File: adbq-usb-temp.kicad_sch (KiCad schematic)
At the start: 74 parts, among them J4 USB_C_Receptacle_USB2.0_14P, Q1 Q_NMOS, Q2 Q_NMOS, Q3 Q_NMOS, SW1 SW_Push, SW2 TestPoint, SW3 TestPoint, SW4 TestPoint, U1 ESP32-S3FH4R2, U14 TMP117AIDRV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

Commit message: schem: update MOSFETs pin numbers
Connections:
- net GND: now also Q1.2 (S), Q2.2 (S), Q3.2 (S); no longer Q1.S, Q2.S, Q3.S
- net at R15.1: now also Q1.1 (G); no longer Q1.G
- net at R11.1: now also Q3.1 (G); no longer Q3.G
- net at U3.8 (DIG3): now also Q3.3 (D); no longer Q3.D
- net at U3.12 (DIG1): now also Q1.3 (D); no longer Q1.D
- net at U3.9 (DIG2): now also Q2.3 (D); no longer Q2.D
- net at R9.1: now also Q2.1 (G); no longer Q2.G
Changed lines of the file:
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@@
 	)
 	(symbol
-		(lib_id "Device:Q_NMOS")
-		(at 111.76 111.76 0)
-		(mirror y)
-		(unit 1)
-		(exclude_from_sim no)
-		(in_bom yes)
-		(on_board yes)
-		(dnp no)
-		(property "Reference" "Q3"
-			(at 107.188 108.966 0)
-			(effects
-				(font
-					(size 1.27 1.27)
-				)
-				(justify left)
-			)
-		)
-		(property "Value" "Q_NMOS"
-			(at 105.41 113.0299 0)
-			(effects
-				(font
-					(size 1.27 1.27)
-				)
-				(justify left)
-				(hide yes)
-			)
-		)
-		(property "Footprint" "Package_TO_SOT_SMD:SOT-323_SC-70"
-			(at 106.68 109.22 0)
-			(effects
-				(font
-					(size 1.27 1.27)
-				)
-				(hide yes)
-			)
-		)
-		(property "Datasheet" "~"
-			(at 111.76 111.76 0)
-			(effects
-				(font
-					(size 1.27 1.27)
-				)
-				(hide yes)
-			)
-		)
-		(property "Description" "N-MOSFET transistor"
-			(at 111.76 111.76 0)
-			(effects
-				(font
-					(size 1.27 1.27)
-				)
-				(hide yes)
-			)
-		)
-		(property "Basic" "E"
-			(at 111.76 111.76 0)
-			(effects
-				(font
-					(size 1.27 1.27)
-				)
-				(hide yes)
-			)
-		)
-		(property "JLCPCB Part #" "C28646265"
-			(at 111.76 111.76 0)
-			(effects
-				(font
-					(size 1.27 1.27)
-				)
-				(hide yes)
-			)
-		)
-		(property "Manufacturer" "hongjiacheng"
-			(at 111.76 111.76 0)
-			(effects
-				(font
-					(size 1.27 1.27)
-				)
-				(hide yes)
-			)
-		)
-		(property "Manufacturer Part Number" "BSS138W"
-			(at 111.76 111.76 0)
-			(effects
-				(font
-					(size 1.27 1.27)
-				)
-				(hide yes)
-			)
-		)
-		(pin "S"
-		)
-		(pin "G"
-		)
-		(pin "D"
-		)
-		(instances
-			(project "adbq-usb-temp"
-				(path "/683f6451-7bb7-4686-955a-dbaefe964302"
-					(reference "Q3")
-					(unit 1)
-				)
-			)
-		)
-	)
-	(symbol
 		(lib_id "power:GND")
 		(at 31.75 190.5 0)
@@
 	)
 	(symbol
+		(lib_id "Device:Q_NMOS")
+		(at 111.76 111.76 0)
+		(mirror y)
+		(unit 1)
+		(exclude_from_sim no)
+		(in_bom yes)
+		(on_board yes)
+		(dnp no)
+		(property "Reference" "Q3"
+			(at 107.188 108.966 0)
+			(effects
+				(font
+					(size 1.27 1.27)
+				)
+				(justify left)
+			)
+		)
+		(property "Value" "Q_NMOS"
+			(at 105.41 113.0299 0)
+			(effects
+				(font
+					(size 1.27 1.27)
+				)
+				(justify left)
+				(hide yes)
+			)
+		)
+		(property "Footprint" "Package_TO_SOT_SMD:SOT-323_SC-70"
+			(at 106.68 109.22 0)
+			(effects
+				(font
+					(size 1.27 1.27)
+				)
+				(hide yes)
+			)
+		)
+		(property "Datasheet" "~"
+			(at 111.76 111.76 0)
+			(effects
+				(font
+					(size 1.27 1.27)
+				)
+				(hide yes)
+			)
+		)
+		(property "Description" "N-MOSFET transistor"
+			(at 111.76 111.76 0)
+			(effects
+				(font
+					(size 1.27 1.27)
+				)
+				(hide yes)
+			)
+		)
+		(property "Basic" "E"
+			(at 111.76 111.76 0)
+			(effects
+				(font
+					(size 1.27 1.27)
+				)
+				(hide yes)
+			)
+		)
+		(property "JLCPCB Part #" "C28646265"
+			(at 111.76 111.76 0)
+			(effects
+				(font
+					(size 1.27 1.27)
+				)
+				(hide yes)
+			)
+		)
+		(property "Manufacturer" "hongjiacheng"
+			(at 111.76 111.76 0)
+			(effects
+				(font
+					(size 1.27 1.27)
+				)
+				(hide yes)
+			)
+		)
+		(property "Manufacturer Part Number" "BSS138W"
+			(at 111.76 111.76 0)
+			(effects
+				(font
+					(size 1.27 1.27)
+				)
+				(hide yes)
+			)
+		)
+		(pin "3"
+		)
+		(pin "2"
+		)
+		(pin "1"
+		)
+		(instances
+			(project "adbq-usb-temp"
+				(path "/683f6451-7bb7-4686-955a-dbaefe964302"
+					(reference "Q3")
+					(unit 1)
+				)
+			)
+		)
+	)
+	(symbol
 		(lib_id "power:GND")
 		(at 38.1 50.8 0)
@@
 			)
 		)
-		(pin "S"
+		(pin "3"
 		)
-		(pin "G"
+		(pin "2"
 		)
-		(pin "D"
+		(pin "1"
 		)
 		(instances
@@
 	)
 	(symbol
+		(lib_id "Device:Q_NMOS")
+		(at 97.79 111.76 0)
+		(mirror y)
+		(unit 1)
+		(exclude_from_sim no)
+		(in_bom yes)
+		(on_board yes)
+		(dnp no)
+		(property "Reference" "Q2"
+			(at 93.218 108.966 0)
+			(effects
+				(font
+					(size 1.27 1.27)
+				)
+				(justify left)
+			)
+		)
+		(property "Value" "Q_NMOS"
+			(at 91.44 113.0299 0)
+			(effects
+				(font
+					(size 1.27 1.27)
+				)
+				(justify left)
+				(hide yes)
+			)
+		)
+		(property "Footprint" "Package_TO_SOT_SMD:SOT-323_SC-70"
+			(at 92.71 109.22 0)
+			(effects
+				(font
+					(size 1.27 1.27)
+				)
+				(hide yes)
+			)
+		)
+		(property "Datasheet" "~"
+			(at 97.79 111.76 0)
+			(effects
+				(font
+					(size 1.27 1.27)
+				)
+				(hide yes)
+			)
+		)
+		(property "Description" "N-MOSFET transistor"
+			(at 97.79 111.76 0)
+			(effects
+				(font
+					(size 1.27 1.27)
+				)
+				(hide yes)
+			)
+		)
+		(property "Basic" "E"
+			(at 97.79 111.76 0)
+			(effects
+				(font
+					(size 1.27 1.27)
+				)
+				(hide yes)
+			)
+		)
+		(property "JLCPCB Part #" "C28646265"
+			(at 97.79 111.76 0)
+			(effects
+				(font
+					(size 1.27 1.27)
+				)
+				(hide yes)
+			)
+		)
+		(property "Manufacturer" "hongjiacheng"
+			(at 97.79 111.76 0)
+			(effects
+				(font
+					(size 1.27 1.27)
+				)
+				(hide yes)
+			)
+		)
+		(property "Manufacturer Part Number" "BSS138W"
+			(at 97.79 111.76 0)
+			(effects
+				(font
+					(size 1.27 1.27)
+				)
+				(hide yes)
+			)
+		)
+		(pin "3"
+		)
+		(pin "2"
+		)
+		(pin "1"
+		)
+		(instances
+			(project "adbq-usb-temp"
+				(path "/683f6451-7bb7-4686-955a-dbaefe964302"
+					(reference "Q2")
+					(unit 1)
+				)
+			)
+		)
+	)
+	(symbol
 		(lib_id "Device:C")
 		(at 133.35 44.45 270)
@@
 					(unit 1)
 				)
-			)
-		)
-	)
-	(symbol
-		(lib_id "Device:Q_NMOS")
-		(at 97.79 111.76 0)
-		(mirror y)
-		(unit 1)
-		(exclude_from_sim no)
-		(in_bom yes)
-		(on_board yes)
-		(dnp no)
-		(property "Reference" "Q2"
-			(at 93.218 108.966 0)
-			(effects
-				(font
-					(size 1.27 1.27)
-				)
-				(justify left)
-			)
-		)
-		(property "Value" "Q_NMOS"
-			(at 91.44 113.0299 0)
-			(effects
-				(font
-					(size 1.27 1.27)
-				)
-				(justify left)
-				(hide yes)
-			)
-		)
-		(property "Footprint" "Package_TO_SOT_SMD:SOT-323_SC-70"
-			(at 92.71 109.22 0)
-			(effects
-				(font
-					(size 1.27 1.27)
-				)
-				(hide yes)
-			)
-		)
-		(property "Datasheet" "~"
-			(at 97.79 111.76 0)
-			(effects
-				(font
-					(size 1.27 1.27)
-				)
-				(hide yes)
-			)
-		)
-		(property "Description" "N-MOSFET transistor"
-			(at 97.79 111.76 0)
-			(effects
-				(font
-					(size 1.27 1.27)
-				)
-				(hide yes)
-			)
-		)
-		(property "Basic" "E"
-			(at 97.79 111.76 0)
-			(effects
-				(font
-					(size 1.27 1.27)
-				)
-				(hide yes)
-			)
-		)
-		(property "JLCPCB Part #" "C28646265"
-			(at 97.79 111.76 0)
-			(effects
-				(font
-					(size 1.27 1.27)
-				)
-				(hide yes)
-			)
-		)
-		(property "Manufacturer" "hongjiacheng"
-			(at 97.79 111.76 0)
-			(effects
-				(font
-					(size 1.27 1.27)
-				)
-				(hide yes)
-			)
-		)
-		(property "Manufacturer Part Number" "BSS138W"
-			(at 97.79 111.76 0)
-			(effects
-				(font
-					(size 1.27 1.27)
-				)
-				(hide yes)
-			)
-		)
-		(pin "S"
-		)
-		(pin "G"
-		)
-		(pin "D"
-		)
-		(instances
-			(project "adbq-usb-temp"
-				(path "/683f6451-7bb7-4686-955a-dbaefe964302"
-					(reference "Q2")
-					(unit 1)
-				)

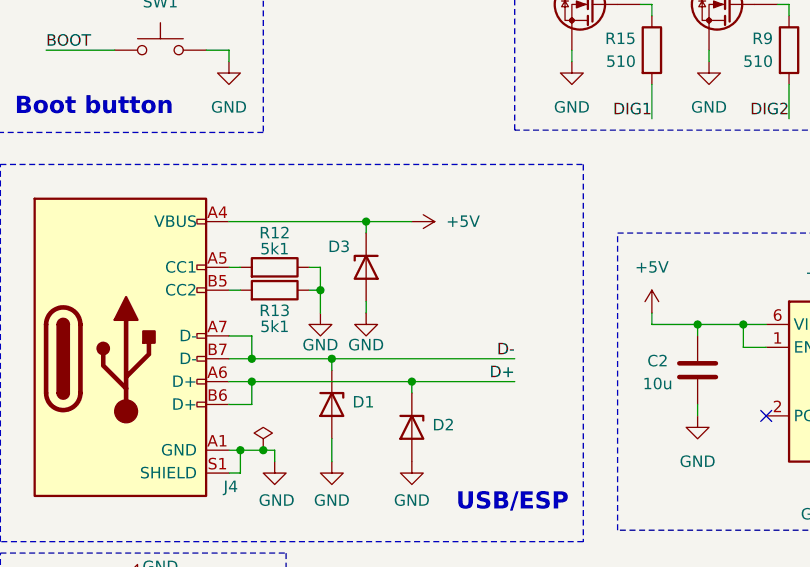
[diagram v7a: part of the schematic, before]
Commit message: pcb: add missing 3d models
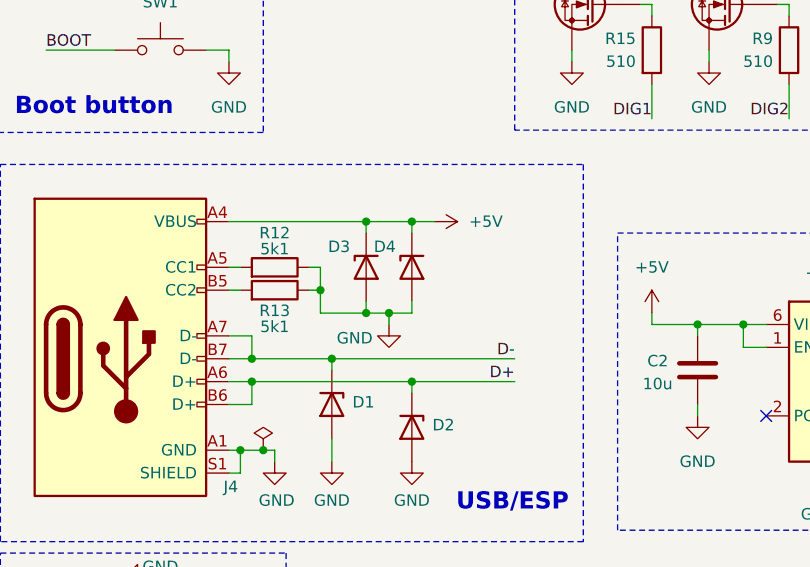
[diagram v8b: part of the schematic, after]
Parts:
- added D4: H5VU10U, Pers:Diode_DFN1006, symbol Pers:H5VU10U
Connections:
- net +5V: now also D4.1 (K)
- net GND: now also D4.2 (A)
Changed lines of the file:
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@@
 	)
 	(junction
+		(at 62.23 135.89)
+		(diameter 0)
+		(color 0 0 0 0)
+	)
+	(junction
 		(at 148.59 158.75)
 		(diameter 0)
@@
 		(color 0 0 0 0)
 	)
+	(junction
+		(at 59.69 146.05)
+		(diameter 0)
+		(color 0 0 0 0)
+	)
+	(junction
+		(at 57.15 146.05)
+		(diameter 0)
+		(color 0 0 0 0)
+	)
 	(no_connect
 		(at 232.41 95.25)
@@
 	(wire
 		(pts
+			(xy 59.69 146.05) (xy 62.23 146.05)
+		)
+		(stroke
+			(width 0)
+			(type default)
+		)
+	)
+	(wire
+		(pts
 			(xy 45.72 161.29) (xy 46.99 161.29)
 		)
@@
 	(wire
 		(pts
+			(xy 59.69 147.32) (xy 59.69 146.05)
+		)
+		(stroke
+			(width 0)
+			(type default)
+		)
+	)
+	(wire
+		(pts
 			(xy 25.4 41.91) (xy 27.94 41.91)
 		)
@@
 	(wire
 		(pts
+			(xy 57.15 146.05) (xy 59.69 146.05)
+		)
+		(stroke
+			(width 0)
+			(type default)
+		)
+	)
+	(wire
+		(pts
 			(xy 31.75 190.5) (xy 31.75 189.23)
 		)
@@
 	(wire
 		(pts
+			(xy 52.07 146.05) (xy 57.15 146.05)
+		)
+		(stroke
+			(width 0)
+			(type default)
+		)
+	)
+	(wire
+		(pts
 			(xy 219.71 49.53) (xy 207.01 49.53)
 		)
@@
 	(wire
 		(pts
+			(xy 62.23 144.78) (xy 62.23 146.05)
+		)
+		(stroke
+			(width 0)
+			(type default)
+		)
+	)
+	(wire
+		(pts
+			(xy 62.23 135.89) (xy 62.23 137.16)
+		)
+		(stroke
+			(width 0)
+			(type default)
+		)
+	)
+	(wire
+		(pts
 			(xy 44.45 156.21) (xy 44.45 153.67)
 		)
@@
 	(wire
 		(pts
+			(xy 62.23 135.89) (xy 64.77 135.89)
+		)
+		(stroke
+			(width 0)
+			(type default)
+		)
+	)
+	(wire
+		(pts
 			(xy 172.72 38.1) (xy 182.88 38.1)
 		)
@@
 	)
 	(symbol
-		(lib_id "power:GND")
-		(at 57.15 146.05 0)
-		(mirror y)
-		(unit 1)
-		(exclude_from_sim no)
-		(in_bom yes)
-		(on_board yes)
-		(dnp no)
-		(property "Reference" "#PWR07"
-			(at 57.15 152.4 0)
-			(effects
-				(font
-					(size 1.27 1.27)
-				)
-				(hide yes)
-			)
-		)
-		(property "Value" "GND"
-			(at 57.15 149.606 0)
-			(effects
-				(font
-					(size 1.27 1.27)
-				)
-			)
-		)
-		(property "Footprint" ""
-			(at 57.15 146.05 0)
-			(effects
-				(font
-					(size 1.27 1.27)
-				)
-				(hide yes)
-			)
-		)
-		(property "Datasheet" ""
-			(at 57.15 146.05 0)
-			(effects
-				(font
-					(size 1.27 1.27)
-				)
-				(hide yes)
-			)
-		)
-		(property "Description" "Power symbol creates a global label with name \"GND\" , ground"
-			(at 57.15 146.05 0)
-			(effects
-				(font
-					(size 1.27 1.27)
-				)
-				(hide yes)
-			)
-		)
-		(pin "1"
-		)
-		(instances
-			(project "adbq-usb-temp"
-				(path "/683f6451-7bb7-4686-955a-dbaefe964302"
-					(reference "#PWR07")
-					(unit 1)
-				)
-			)
-		)
-	)
-	(symbol
 		(lib_id "Connector:TestPoint")
 		(at 245.11 90.17 270)
@@
 	)
 	(symbol
+		(lib_id "Pers:H5VU10U")
+		(at 62.23 140.97 90)
+		(mirror x)
+		(unit 1)
+		(exclude_from_sim no)
+		(in_bom yes)
+		(on_board yes)
+		(dnp no)
+		(property "Reference" "D4"
+			(at 60.452 138.684 90)
+			(effects
+				(font
+					(size 1.27 1.27)
+				)
+				(justify left)
+			)
+		)
+		(property "Value" "H5VU10U"
+			(at 59.69 142.2399 90)
+			(effects
+				(font
+					(size 1.27 1.27)
+				)
+				(justify left)
+				(hide yes)
+			)
+		)
+		(property "Footprint" "Pers:Diode_DFN1006"
+			(at 66.675 140.97 0)
+			(effects
+				(font
+					(size 1.27 1.27)
+				)
+				(hide yes)
+			)
+		)
+		(property "Datasheet" "https://datasheet.lcsc.com/lcsc/2504101957_hongjiacheng-H5VU10U_C22395519.pdf"
+			(at 62.23 140.97 0)
+			(effects
+				(font
+					(size 1.27 1.27)
+				)
+				(hide yes)
+			)
+		)
+		(property "Description" "-55℃~+155℃ 0.8pF 16V 200nA 55W@8/20us 5A@8/20us 5V 6V ESD IEC 61000-4-2 Unidirectional DFN1006-2L ESD and Surge Protection (TVS/ESD) ROHS"
+			(at 62.23 140.97 0)
+			(effects
+				(font
+					(size 1.27 1.27)
+				)
+				(hide yes)
+			)
+		)
+		(property "Basic" "E"
+			(at 62.23 140.97 90)
+			(effects
+				(font
+					(size 1.27 1.27)
+				)
+				(hide yes)
+			)
+		)
+		(property "JLCPCB Part #" "C22395519"
+			(at 62.23 140.97 90)
+			(effects
+				(font
+					(size 1.27 1.27)
+				)
+				(hide yes)
+			)
+		)
+		(property "Manufacturer" "hongjiacheng"
+			(at 62.23 140.97 90)
+			(effects
+				(font
+					(size 1.27 1.27)
+				)
+				(hide yes)
+			)
+		)
+		(property "Manufacturer Part Number" "H5VU10U"
+			(at 62.23 140.97 90)
+			(effects
+				(font
+					(size 1.27 1.27)
+				)
+				(hide yes)
+			)
+		)
+		(pin "1"
+		)
+		(pin "2"
+		)
+		(instances
+			(project "adbq-usb-temp"
+				(path "/683f6451-7bb7-4686-955a-dbaefe964302"
+					(reference "D4")
+					(unit 1)
+				)
+			)
+		)
+	)
+	(symbol
 		(lib_id "Switch:SW_Push")
 		(at 34.29 116.84 0)
@@
 	)
 	(symbol
+		(lib_id "power:GND")
+		(at 59.69 147.32 0)
+		(mirror y)
+		(unit 1)
+		(exclude_from_sim no)
+		(in_bom yes)
+		(on_board yes)
+		(dnp no)
+		(property "Reference" "#PWR029"
+			(at 59.69 153.67 0)
+			(effects
+				(font
+					(size 1.27 1.27)
+				)
+				(hide yes)
+			)
+		)
+		(property "Value" "GND"
+			(at 55.88 148.844 0)
+			(effects
+				(font
+					(size 1.27 1.27)
+				)
+			)
+		)
+		(property "Footprint" ""
+			(at 59.69 147.32 0)
+			(effects
+				(font
+					(size 1.27 1.27)
+				)
+				(hide yes)
+			)
+		)
+		(property "Datasheet" ""
+			(at 59.69 147.32 0)
+			(effects
+				(font
+					(size 1.27 1.27)
+				)
+				(hide yes)
+			)
+		)
+		(property "Description" "Power symbol creates a global label with name \"GND\" , ground"
+			(at 59.69 147.32 0)
+			(effects
+				(font
+					(size 1.27 1.27)
+				)
+				(hide yes)
+			)
+		)
+		(pin "1"
+		)
+		(instances
+			(project "adbq-usb-temp"
+				(path "/683f6451-7bb7-4686-955a-dbaefe964302"
+					(reference "#PWR029")
+					(unit 1)
+				)
+			)
+		)
+	)
+	(symbol
 		(lib_id "Device:Q_NMOS")
 		(at 111.76 111.76 0)
@@
 	)
 	(symbol
-		(lib_id "power:GND")
-		(at 52.07 146.05 0)
-		(mirror y)
-		(unit 1)
-		(exclude_from_sim no)
-		(in_bom yes)
-		(on_board yes)
-		(dnp no)
-		(property "Reference" "#PWR047"
-			(at 52.07 152.4 0)
-			(effects
-				(font
-					(size 1.27 1.27)
-				)
-				(hide yes)
-			)
-		)
-		(property "Value" "GND"
-			(at 52.07 149.606 0)
-			(effects
-				(font
-					(size 1.27 1.27)
-				)
-			)
-		)
-		(property "Footprint" ""
-			(at 52.07 146.05 0)
-			(effects
-				(font
-					(size 1.27 1.27)
-				)
-				(hide yes)
-			)
-		)
-		(property "Datasheet" ""
-			(at 52.07 146.05 0)
-			(effects
-				(font
-					(size 1.27 1.27)
-				)
-				(hide yes)
-			)
-		)
-		(property "Description" "Power symbol creates a global label with name \"GND\" , ground"
-			(at 52.07 146.05 0)
-			(effects
-				(font
-					(size 1.27 1.27)
-				)
-				(hide yes)
-			)
-		)
-		(pin "1"
-		)
-		(instances
-			(project "adbq-usb-temp"
-				(path "/683f6451-7bb7-4686-955a-dbaefe964302"
-					(reference "#PWR047")
-					(unit 1)
-				)
-			)
-		)
-	)
-	(symbol
 		(lib_id "power:+3V3")
 		(at 257.81 71.12 0)
@@
 	(symbol
 		(lib_id "power:+5V")
-		(at 62.23 135.89 270)
+		(at 64.77 135.89 270)
 		(mirror x)
 		(unit 1)
@@
 		(fields_autoplaced yes)
 		(property "Reference" "#PWR044"
-			(at 58.42 135.89 0)
+			(at 60.96 135.89 0)
 			(effects
 				(font
@@
 		)
 		(property "Value" "+5V"
-			(at 66.04 135.8899 90)
+			(at 68.58 135.8899 90)
 			(effects
 				(font
@@
 		)
 		(property "Footprint" ""
-			(at 62.23 135.89 0)
+			(at 64.77 135.89 0)
 			(effects
 				(font
@@
 		)
 		(property "Datasheet" ""
-			(at 62.23 135.89 0)
+			(at 64.77 135.89 0)
 			(effects
 				(font
@@
 		)
 		(property "Description" "Power symbol creates a global label with name \"+5V\""
-			(at 62.23 135.89 0)
+			(at 64.77 135.89 0)
 			(effects
 				(font
